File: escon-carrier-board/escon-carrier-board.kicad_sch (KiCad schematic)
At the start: 3 parts, among them J1 Conn_01x06

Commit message: V.1.0
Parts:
- added H1, H2: MountingHole, MountingHole:MountingHole_2.2mm_M2, symbol Mechanical:MountingHole
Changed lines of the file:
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@@
+	)
+	(symbol
+		(lib_id "Mechanical:MountingHole")
+		(at 39.37 67.31 0)
+		(unit 1)
+		(exclude_from_sim yes)
+		(in_bom no)
+		(on_board yes)
+		(dnp no)
+		(fields_autoplaced yes)
+		(property "Reference" "H1"
+			(at 41.91 66.0399 0)
+			(effects
+				(font
+					(size 1.27 1.27)
+				)
+				(justify left)
+			)
+		)
+		(property "Value" "MountingHole"
+			(at 41.91 68.5799 0)
+			(effects
+				(font
+					(size 1.27 1.27)
+				)
+				(justify left)
+			)
+		)
+		(property "Footprint" "MountingHole:MountingHole_2.2mm_M2"
+			(at 39.37 67.31 0)
+			(effects
+				(font
+					(size 1.27 1.27)
+				)
+			)
+		)
+		(property "Datasheet" "~"
+			(at 39.37 67.31 0)
+			(effects
+				(font
+					(size 1.27 1.27)
+				)
+				(hide yes)
+			)
+		)
+		(property "Description" "Mounting Hole without connection"
+			(at 39.37 67.31 0)
+			(effects
+				(font
+					(size 1.27 1.27)
+				)
+				(hide yes)
+			)
+		)
+		(instances
+			(project ""
+				(path "/92c42422-b927-4b81-be56-0250212e9826"
+					(reference "H1")
+					(unit 1)
+				)
+			)
+		)
+	)
+	(symbol
+		(lib_id "Mechanical:MountingHole")
+		(at 39.37 73.66 0)
+		(unit 1)
+		(exclude_from_sim yes)
+		(in_bom no)
+		(on_board yes)
+		(dnp no)
+		(fields_autoplaced yes)
+		(property "Reference" "H2"
+			(at 41.91 72.3899 0)
+			(effects
+				(font
+					(size 1.27 1.27)
+				)
+				(justify left)
+			)
+		)
+		(property "Value" "MountingHole"
+			(at 41.91 74.9299 0)
+			(effects
+				(font
+					(size 1.27 1.27)
+				)
+				(justify left)
+			)
+		)
+		(property "Footprint" "MountingHole:MountingHole_2.2mm_M2"
+			(at 39.37 73.66 0)
+			(effects
+				(font
+					(size 1.27 1.27)
+				)
+			)
+		)
+		(property "Datasheet" "~"
+			(at 39.37 73.66 0)
+			(effects
+				(font
+					(size 1.27 1.27)
+				)
+				(hide yes)
+			)
+		)
+		(property "Description" "Mounting Hole without connection"
+			(at 39.37 73.66 0)
+			(effects
+				(font
+					(size 1.27 1.27)
+				)
+				(hide yes)
+			)
+		)
+		(instances
+			(project "escon-carrier-board"
+				(path "/92c42422-b927-4b81-be56-0250212e9826"
+					(reference "H2")
+					(unit 1)
+				)
+			)
+		)
 	)
 	(symbol

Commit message: V3.0
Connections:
- net GND: now reaches ESCON1.P18 (GND), ESCON1.P5 (GND), J1.6 (Pin_6), JP1.4

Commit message: V5.0
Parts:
- added H3, H4: MountingHole, MountingHole:MountingHole_2.2mm_M2, symbol Mechanical:MountingHole
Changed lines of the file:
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@@
+	)
+	(symbol
+		(lib_id "Mechanical:MountingHole")
+		(at 39.37 86.36 0)
+		(unit 1)
+		(exclude_from_sim yes)
+		(in_bom no)
+		(on_board yes)
+		(dnp no)
+		(fields_autoplaced yes)
+		(property "Reference" "H4"
+			(at 41.91 85.0899 0)
+			(effects
+				(font
+					(size 1.27 1.27)
+				)
+				(justify left)
+			)
+		)
+		(property "Value" "MountingHole"
+			(at 41.91 87.6299 0)
+			(effects
+				(font
+					(size 1.27 1.27)
+				)
+				(justify left)
+			)
+		)
+		(property "Footprint" "MountingHole:MountingHole_2.2mm_M2"
+			(at 39.37 86.36 0)
+			(effects
+				(font
+					(size 1.27 1.27)
+				)
+			)
+		)
+		(property "Datasheet" "~"
+			(at 39.37 86.36 0)
+			(effects
+				(font
+					(size 1.27 1.27)
+				)
+				(hide yes)
+			)
+		)
+		(property "Description" "Mounting Hole without connection"
+			(at 39.37 86.36 0)
+			(effects
+				(font
+					(size 1.27 1.27)
+				)
+				(hide yes)
+			)
+		)
+		(instances
+			(project "escon-carrier-board"
+				(path "/92c42422-b927-4b81-be56-0250212e9826"
+					(reference "H4")
+					(unit 1)
+				)
+			)
+		)
 	)
 	(symbol
@@
 					(unit 1)
 				)
+			)
+		)
+	)
+	(symbol
+		(lib_id "Mechanical:MountingHole")
+		(at 39.37 80.01 0)
+		(unit 1)
+		(exclude_from_sim yes)
+		(in_bom no)
+		(on_board yes)
+		(dnp no)
+		(fields_autoplaced yes)
+		(property "Reference" "H3"
+			(at 41.91 78.7399 0)
+			(effects
+				(font
+					(size 1.27 1.27)
+				)
+				(justify left)
+			)
+		)
+		(property "Value" "MountingHole"
+			(at 41.91 81.2799 0)
+			(effects
+				(font
+					(size 1.27 1.27)
+				)
+				(justify left)
+			)
+		)
+		(property "Footprint" "MountingHole:MountingHole_2.2mm_M2"
+			(at 39.37 80.01 0)
+			(effects
+				(font
+					(size 1.27 1.27)
+				)
+			)
+		)
+		(property "Datasheet" "~"
+			(at 39.37 80.01 0)
+			(effects
+				(font
+					(size 1.27 1.27)
+				)
+				(hide yes)
+			)
+		)
+		(property "Description" "Mounting Hole without connection"
+			(at 39.37 80.01 0)
+			(effects
+				(font
+					(size 1.27 1.27)
+				)
+				(hide yes)
+			)
+		)
+		(instances
+			(project "escon-carrier-board"
+				(path "/92c42422-b927-4b81-be56-0250212e9826"
+					(reference "H3")
+					(unit 1)
+				)

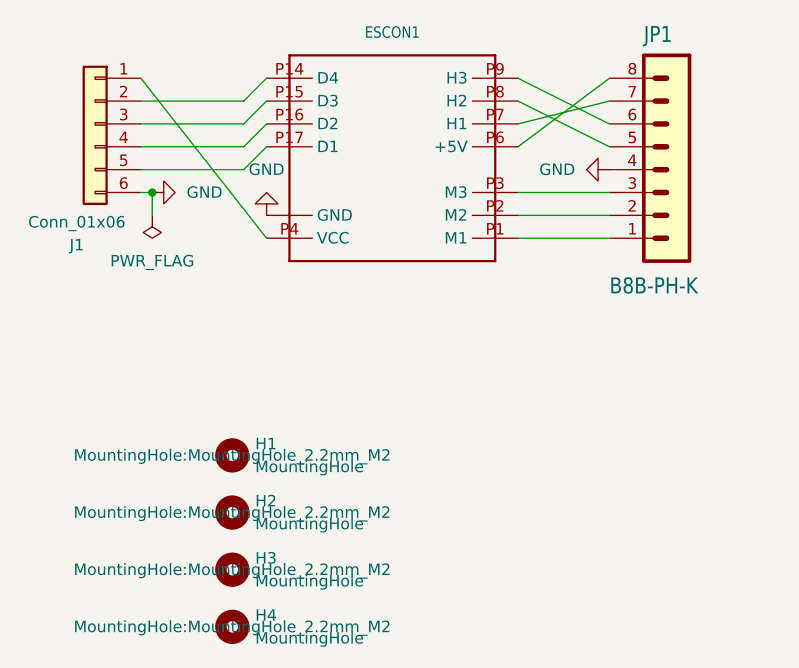
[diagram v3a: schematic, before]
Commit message: Changed to micromatch 10 pole connector
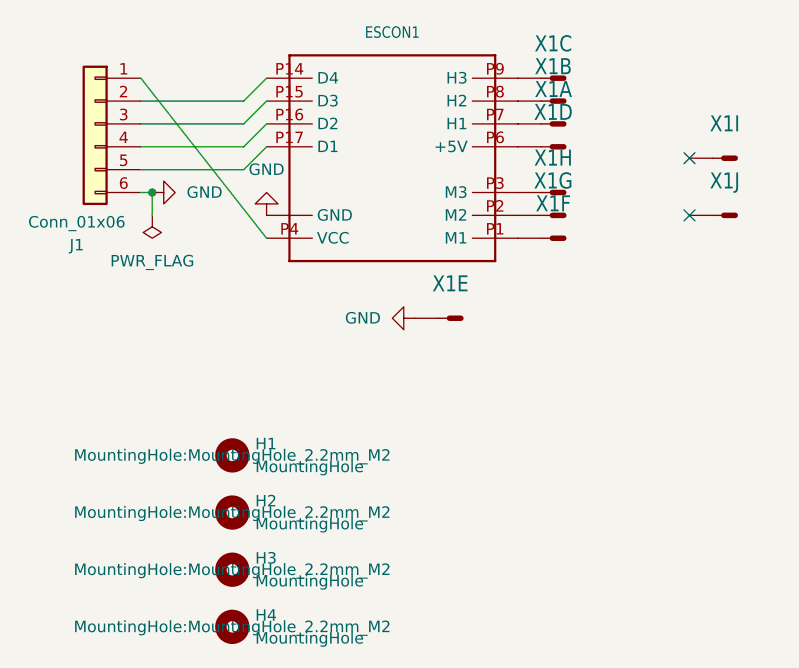
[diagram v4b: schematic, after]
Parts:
- removed JP1: B8B-PH-K, Connector_JST:JST_PH_B8B-PH-K_1x08_P2.00mm_Vertical, symbol main_backupboard-eagle-import:B8B-PH-K
- added X1: ~, BohleBots:MICROMATCH-10, symbol bohlebots.lib:MICROMATCH-10
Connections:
- net GND: now also X1.5 (S)
- net at ESCON1.P1 (M1): now also X1.6 (S)
- net at ESCON1.P2 (M2): now also X1.7 (S)
- net at ESCON1.P3 (M3): now also X1.8 (S)
- net at ESCON1.P6 (+5V): now also X1.4 (S)
- net at ESCON1.P7 (H1): now also X1.1 (S)
- net at ESCON1.P8 (H2): now also X1.2 (S)
- net at ESCON1.P9 (H3): now also X1.3 (S)
- no-connect marks 0 -> 2

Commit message: Gerber Files
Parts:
- removed H3, H4: MountingHole, MountingHole:MountingHole_2.2mm_M2, symbol Mechanical:MountingHole
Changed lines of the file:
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@@
 		(on_board yes)
 		(dnp no)
-		(fields_autoplaced yes)
 		(property "Reference" "X1"
-			(at 75.0443 26.67 0)
+			(at 78.74 30.48 0)
 			(effects
 				(font
@@
 		(on_board yes)
 		(dnp no)
-		(fields_autoplaced yes)
 		(property "Reference" "X1"
-			(at 75.0443 36.83 0)
+			(at 78.74 40.64 0)
 			(effects
 				(font
@@
 		(on_board yes)
 		(dnp no)
-		(fields_autoplaced yes)
 		(property "Reference" "X1"
-			(at 94.0943 30.48 0)
+			(at 97.79 34.29 0)
 			(effects
 				(font
@@
 		(on_board yes)
 		(dnp no)
-		(fields_autoplaced yes)
 		(property "Reference" "X1"
-			(at 75.0443 39.37 0)
+			(at 78.74 43.18 0)
 			(effects
 				(font
@@
 		(on_board yes)
 		(dnp no)
-		(fields_autoplaced yes)
 		(property "Reference" "X1"
-			(at 63.6143 48.26 0)
+			(at 67.31 52.07 0)
 			(effects
 				(font
@@
 					(reference "X1")
 					(unit 5)
-				)
-			)
-		)
-	)
-	(symbol
-		(lib_id "Mechanical:MountingHole")
-		(at 39.37 86.36 0)
-		(unit 1)
-		(exclude_from_sim yes)
-		(in_bom no)
-		(on_board yes)
-		(dnp no)
-		(fields_autoplaced yes)
-		(property "Reference" "H4"
-			(at 41.91 85.0899 0)
-			(effects
-				(font
-					(size 1.27 1.27)
-				)
-				(justify left)
-			)
-		)
-		(property "Value" "MountingHole"
-			(at 41.91 87.6299 0)
-			(effects
-				(font
-					(size 1.27 1.27)
-				)
-				(justify left)
-			)
-		)
-		(property "Footprint" "MountingHole:MountingHole_2.2mm_M2"
-			(at 39.37 86.36 0)
-			(effects
-				(font
-					(size 1.27 1.27)
-				)
-			)
-		)
-		(property "Datasheet" "~"
-			(at 39.37 86.36 0)
-			(effects
-				(font
-					(size 1.27 1.27)
-				)
-				(hide yes)
-			)
-		)
-		(property "Description" "Mounting Hole without connection"
-			(at 39.37 86.36 0)
-			(effects
-				(font
-					(size 1.27 1.27)
-				)
-				(hide yes)
-			)
-		)
-		(instances
-			(project "escon-carrier-board"
-				(path "/92c42422-b927-4b81-be56-0250212e9826"
-					(reference "H4")
-					(unit 1)
 				)
 			)
@@
 		(on_board yes)
 		(dnp no)
-		(fields_autoplaced yes)
 		(property "Reference" "X1"
-			(at 75.0443 29.21 0)
+			(at 78.74 33.02 0)
 			(effects
 				(font
@@
 		(on_board yes)
 		(dnp no)
-		(fields_autoplaced yes)
 		(property "Reference" "X1"
-			(at 75.0443 24.13 0)
+			(at 78.74 27.94 0)
 			(effects
 				(font
@@
 		(on_board yes)
 		(dnp no)
-		(fields_autoplaced yes)
 		(property "Reference" "X1"
-			(at 75.0443 34.29 0)
+			(at 78.74 38.1 0)
 			(effects
 				(font
@@
 		(on_board yes)
 		(dnp no)
-		(fields_autoplaced yes)
 		(property "Reference" "X1"
-			(at 75.0443 21.59 0)
+			(at 78.74 25.4 0)
 			(effects
 				(font
@@
 		(on_board yes)
 		(dnp no)
-		(fields_autoplaced yes)
 		(property "Reference" "X1"
-			(at 94.0943 36.83 0)
+			(at 97.79 40.64 0)
 			(effects
 				(font
@@
 				)
 			)
-		)
-	)
-	(symbol
-		(lib_id "Mechanical:MountingHole")
-		(at 39.37 80.01 0)
-		(unit 1)
-		(exclude_from_sim yes)
-		(in_bom no)
-		(on_board yes)
-		(dnp no)
-		(fields_autoplaced yes)
-		(property "Reference" "H3"
-			(at 41.91 78.7399 0)
-			(effects
-				(font
-					(size 1.27 1.27)
-				)
-				(justify left)
-			)
-		)
-		(property "Value" "MountingHole"
-			(at 41.91 81.2799 0)
-			(effects
-				(font
-					(size 1.27 1.27)
-				)
-				(justify left)
-			)
-		)
-		(property "Footprint" "MountingHole:MountingHole_2.2mm_M2"
-			(at 39.37 80.01 0)
-			(effects
-				(font
-					(size 1.27 1.27)
-				)
-			)
-		)
-		(property "Datasheet" "~"
-			(at 39.37 80.01 0)
-			(effects
-				(font
-					(size 1.27 1.27)
-				)
-				(hide yes)
-			)
-		)
-		(property "Description" "Mounting Hole without connection"
-			(at 39.37 80.01 0)
-			(effects
-				(font
-					(size 1.27 1.27)
-				)
-				(hide yes)
-			)
-		)
-		(instances
-			(project "escon-carrier-board"
-				(path "/92c42422-b927-4b81-be56-0250212e9826"
-					(reference "H3")
-					(unit 1)
-				)
-			)
